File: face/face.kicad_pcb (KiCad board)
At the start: 2 copper layers, 84 x 84 mm, 4 parts

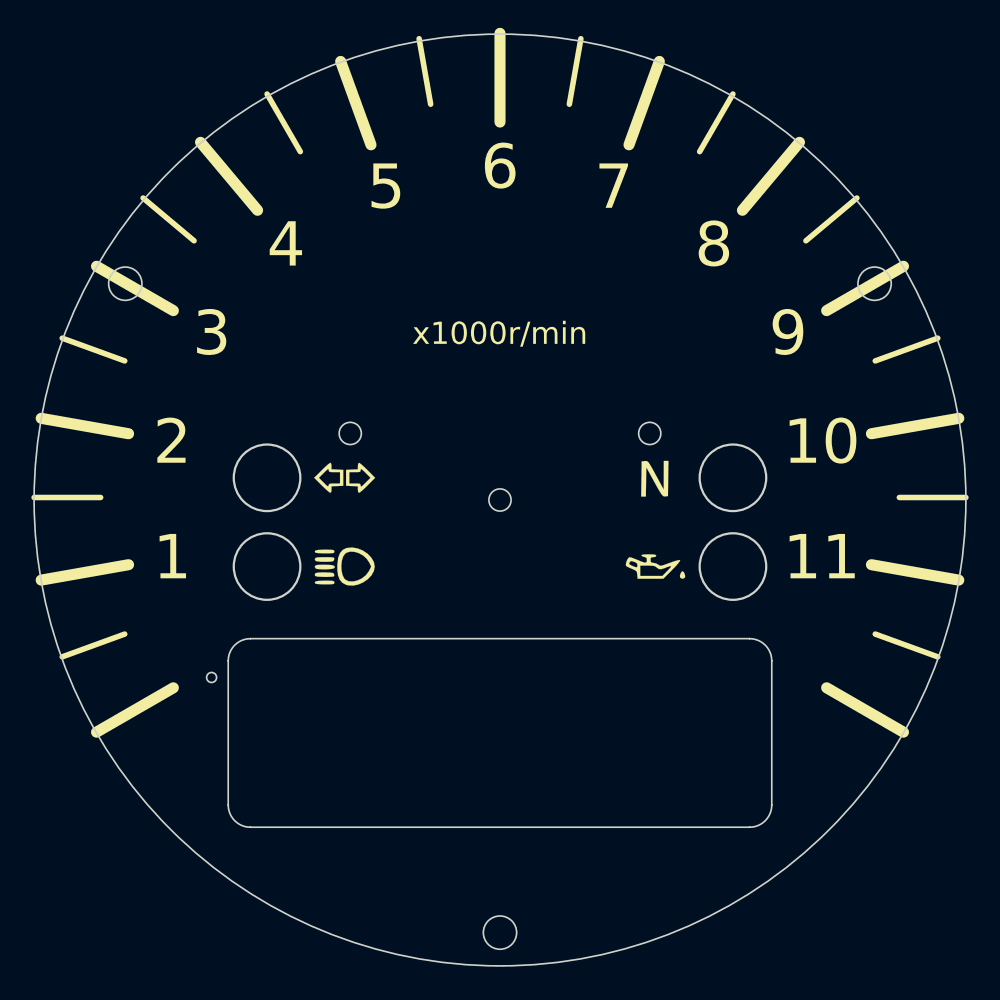
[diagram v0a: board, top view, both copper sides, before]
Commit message: LCD version only
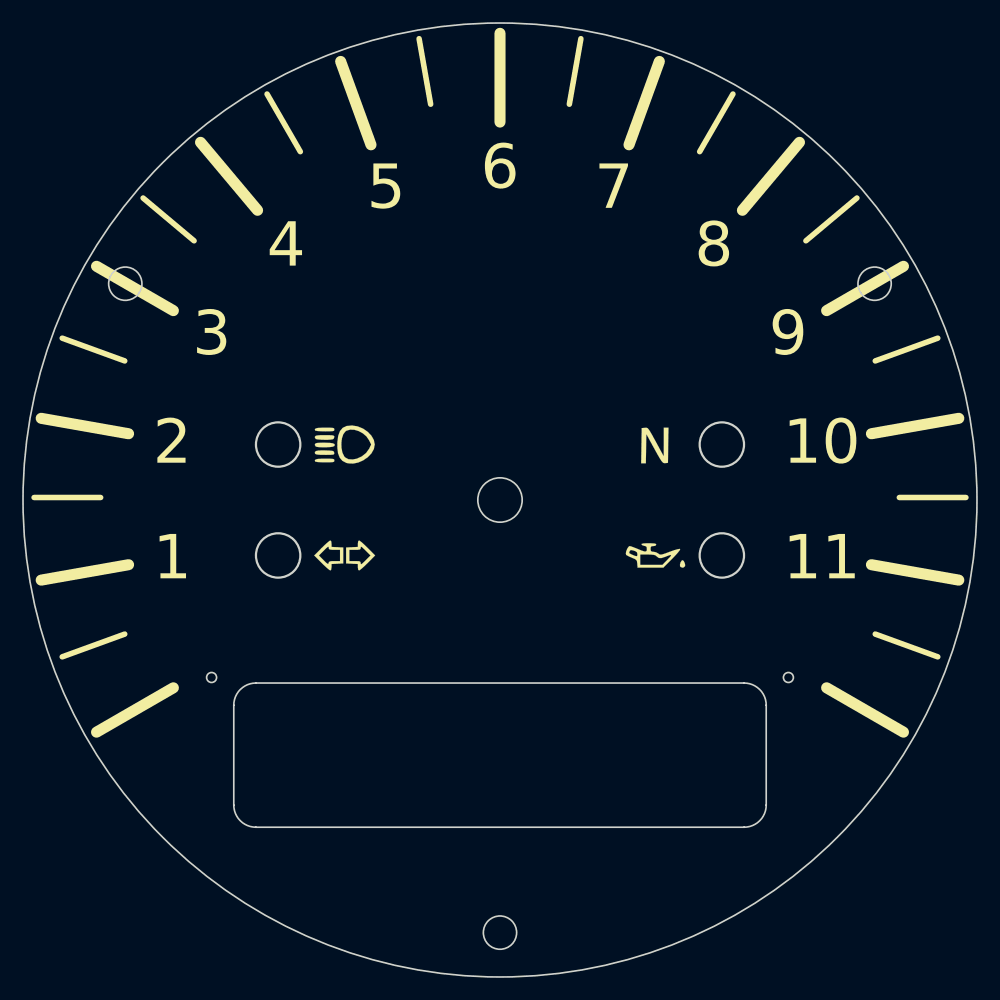
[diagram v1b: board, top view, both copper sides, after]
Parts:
- moved G*** 11.0 mm to (136.0, 95.0)
- moved G*** 7.00 mm to (136.0, 105.0)
- moved G*** 3.00 mm to (164.0, 95.0)
- moved G*** 1.00 mm to (164.0, 105.0)
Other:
- board size 84 x 84 mm -> 86 x 86 mm
- board text removed: "x1000r/min"
